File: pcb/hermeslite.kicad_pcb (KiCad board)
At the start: 4 copper layers, 49.9 x 49.9 mm, 71 parts, among them CN1 MEC6-140_CONNECTOR_BEMICRO, CN2 PCIE, CN4 SATA22, J1 0, J2 0, J3 0, J4 0, J5 0, P0 CONN_1, P12 CONN_1, P3 3V, P5 CONN_1, U1 AD9866BCPZ, U2 EEPROM, X1 61.440

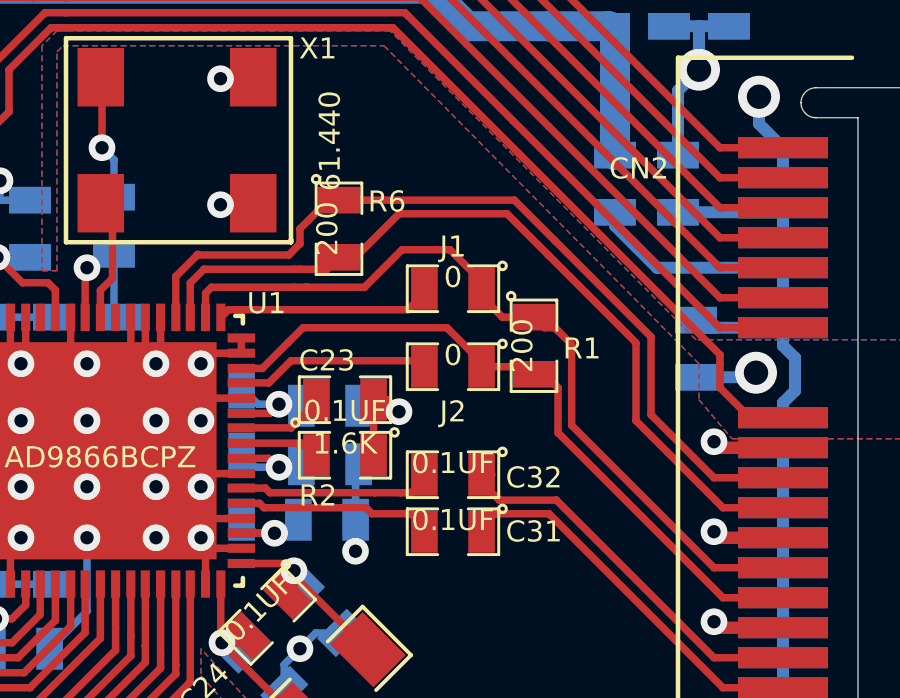
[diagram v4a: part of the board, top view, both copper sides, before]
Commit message: Updated BOM, renumbered a few references
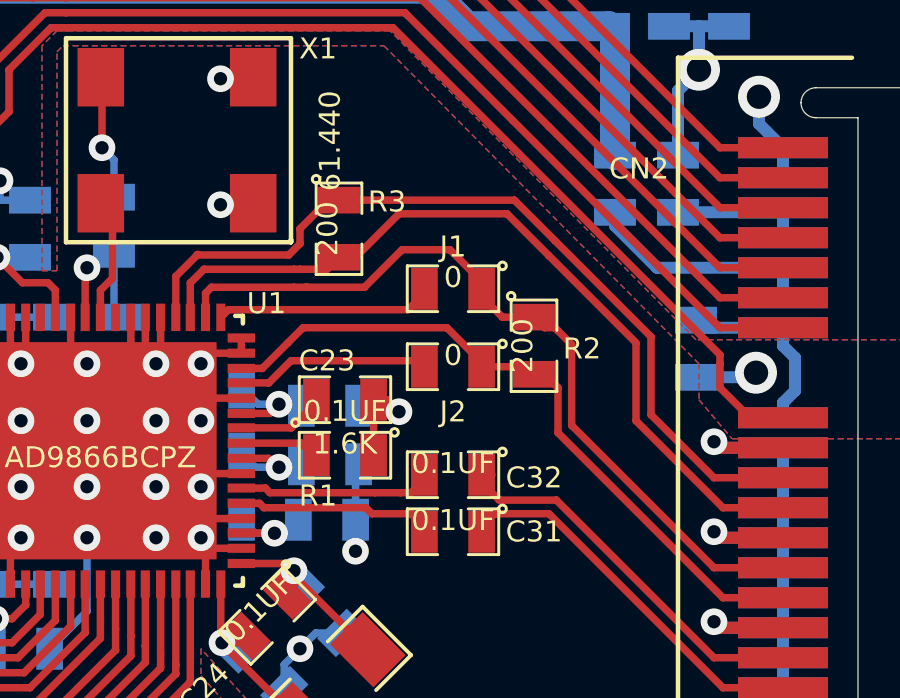
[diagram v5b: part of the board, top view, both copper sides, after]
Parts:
- P3: value 3V -> CONN_1
- renumbered CN4 to CN3, R2 to R1, R1 to R2, R6 to R3

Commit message: iTead Studio submission
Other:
- net class Default: clearance 0.205 -> 0
- rule trace_clearance: 0.205 -> 0
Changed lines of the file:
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@@
   (title_block
     (title Hermes-Lite)
-    (date "07 Oct 2014")
+    (date "08 Oct 2014")
     (rev 1,2)
     (company SofterHardware)
@@
   (layers
     (0 F.Cu signal)
-    (1 Inner2.Cu signal hide)
-    (2 Inner1.Cu signal hide)
-    (31 B.Cu signal hide)
+    (1 Inner2.Cu signal)
+    (2 Inner1.Cu signal)
+    (31 B.Cu signal)
     (32 B.Adhes user)
     (33 F.Adhes user)
@@
     (35 F.Paste user)
     (36 B.SilkS user)
-    (37 F.SilkS user hide)
+    (37 F.SilkS user)
     (38 B.Mask user)
     (39 F.Mask user)
@@
     (user_trace_width 0.4)
     (user_trace_width 1)
-    (trace_clearance 0.205)
+    (trace_clearance 0)
     (zone_clearance 0.45)
     (zone_45_only no)
@@
     (pad_drill 0.813)
     (pad_to_mask_clearance 0)
-    (aux_axis_origin 100.7 83.45)
+    (aux_axis_origin 100.7 83.2)
     (visible_elements FFFEFF7F)
     (pcbplotparams
-      (layerselection 0x01030_80000007)
+      (layerselection 0x010f0_80000007)
       (usegerberextensions true)
-      (excludeedgelayer true)
+      (excludeedgelayer false)
       (linewidth 0.150000)
       (plotframeref false)
@@
   (net 94 "Net-(R1-Pad2)")
   (net_class Default "This is the default net class."
-    (clearance 0.205)
+    (clearance 0)
     (trace_width 0.25)
     (via_dia 0.889)
@@
     (pad B18 smd rect (at -7.5 3.5 270) (size 0.7 3) (layers F.Cu F.Paste F.Mask)
       (net 81 /EXP_SCLK))
-    (pad A1 smd rect (at 11.5 3.5 270) (size 0.7 3) (layers B.Cu F.Paste F.Mask)
-      (net 5 GND))
-    (pad A2 smd rect (at 10.5 3.5 270) (size 0.7 3) (layers B.Cu F.Paste F.Mask)
-      (net 5 GND))
-    (pad A3 smd rect (at 9.5 3.5 270) (size 0.7 3) (layers B.Cu F.Paste F.Mask)
-      (net 5 GND))
-    (pad A4 smd rect (at 8.5 3.5 270) (size 0.7 3) (layers B.Cu F.Paste F.Mask)
-      (net 5 GND))
-    (pad A5 smd rect (at 7.5 3.5 270) (size 0.7 3) (layers B.Cu F.Paste F.Mask)
-      (net 5 GND))
-    (pad A6 smd rect (at 6.5 3.5 270) (size 0.7 3) (layers B.Cu F.Paste F.Mask)
-      (net 5 GND))
-    (pad A7 smd rect (at 5.5 3.5 270) (size 0.7 3) (layers B.Cu F.Paste F.Mask)
-      (net 5 GND))
-    (pad A8 smd rect (at 4.5 3.5 270) (size 0.7 3) (layers B.Cu F.Paste F.Mask)
-      (net 5 GND))
-    (pad A9 smd rect (at 3.5 3.5 270) (size 0.7 3) (layers B.Cu F.Paste F.Mask)
-      (net 5 GND))
-    (pad A10 smd rect (at 2.5 3.5 270) (size 0.7 3) (layers B.Cu F.Paste F.Mask)
-      (net 5 GND))
-    (pad A11 smd rect (at 1.5 3.5 270) (size 0.7 3) (layers B.Cu F.Paste F.Mask)
+    (pad A1 smd rect (at 11.5 3.5 270) (size 0.7 3) (layers B.Cu B.Paste B.Mask)
+      (net 5 GND))
+    (pad A2 smd rect (at 10.5 3.5 270) (size 0.7 3) (layers B.Cu B.Paste B.Mask)
+      (net 5 GND))
+    (pad A3 smd rect (at 9.5 3.5 270) (size 0.7 3) (layers B.Cu B.Paste B.Mask)
+      (net 5 GND))
+    (pad A4 smd rect (at 8.5 3.5 270) (size 0.7 3) (layers B.Cu B.Paste B.Mask)
+      (net 5 GND))
+    (pad A5 smd rect (at 7.5 3.5 270) (size 0.7 3) (layers B.Cu B.Paste B.Mask)
+      (net 5 GND))
+    (pad A6 smd rect (at 6.5 3.5 270) (size 0.7 3) (layers B.Cu B.Paste B.Mask)
+      (net 5 GND))
+    (pad A7 smd rect (at 5.5 3.5 270) (size 0.7 3) (layers B.Cu B.Paste B.Mask)
+      (net 5 GND))
+    (pad A8 smd rect (at 4.5 3.5 270) (size 0.7 3) (layers B.Cu B.Paste B.Mask)
+      (net 5 GND))
+    (pad A9 smd rect (at 3.5 3.5 270) (size 0.7 3) (layers B.Cu B.Paste B.Mask)
+      (net 5 GND))
+    (pad A10 smd rect (at 2.5 3.5 270) (size 0.7 3) (layers B.Cu B.Paste B.Mask)
+      (net 5 GND))
+    (pad A11 smd rect (at 1.5 3.5 270) (size 0.7 3) (layers B.Cu B.Paste B.Mask)
       (net 91 EXP12V))
-    (pad A12 smd rect (at -1.5 3.5 270) (size 0.7 3) (layers B.Cu F.Paste F.Mask)
+    (pad A12 smd rect (at -1.5 3.5 270) (size 0.7 3) (layers B.Cu B.Paste B.Mask)
       (net 91 EXP12V))
-    (pad A13 smd rect (at -2.5 3.5 270) (size 0.7 3) (layers B.Cu F.Paste F.Mask)
+    (pad A13 smd rect (at -2.5 3.5 270) (size 0.7 3) (layers B.Cu B.Paste B.Mask)
       (net 92 EXP5V))
-    (pad A14 smd rect (at -3.5 3.5 270) (size 0.7 3) (layers B.Cu F.Paste F.Mask)
+    (pad A14 smd rect (at -3.5 3.5 270) (size 0.7 3) (layers B.Cu B.Paste B.Mask)
       (net 92 EXP5V))
-    (pad A15 smd rect (at -4.5 3.5 270) (size 0.7 3) (layers B.Cu F.Paste F.Mask)
+    (pad A15 smd rect (at -4.5 3.5 270) (size 0.7 3) (layers B.Cu B.Paste B.Mask)
       (net 93 EXP3V))
-    (pad A16 smd rect (at -5.5 3.5 270) (size 0.7 3) (layers B.Cu F.Paste F.Mask)
+    (pad A16 smd rect (at -5.5 3.5 270) (size 0.7 3) (layers B.Cu B.Paste B.Mask)
       (net 93 EXP3V))
-    (pad A17 smd rect (at -6.5 3.5 270) (size 0.7 3) (layers B.Cu F.Paste F.Mask)
-      (net 5 GND))
-    (pad A18 smd rect (at -7.5 3.5 270) (size 0.7 3) (layers B.Cu F.Paste F.Mask)
+    (pad A17 smd rect (at -6.5 3.5 270) (size 0.7 3) (layers B.Cu B.Paste B.Mask)
+      (net 5 GND))
+    (pad A18 smd rect (at -7.5 3.5 270) (size 0.7 3) (layers B.Cu B.Paste B.Mask)
       (net 5 GND))
   )
@@
     (at 130.1 122 90)
     (attr smd)
-    (fp_text reference FB1 (at 2.7 0 180) (layer F.SilkS)
+    (fp_text reference FB1 (at 2.7 -0.4 180) (layer F.SilkS)
       (effects (font (size 0.7 0.7) (thickness 0.1)))
     )
@@
     (at 132.1 122 90)
     (attr smd)
-    (fp_text reference FB2 (at 2.7 0 180) (layer F.SilkS)
+    (fp_text reference FB2 (at 2.7 -0.3 180) (layer F.SilkS)
       (effects (font (size 0.7 0.7) (thickness 0.1)))
     )
@@
     (at 134.1 122 90)
     (attr smd)
-    (fp_text reference FB3 (at 2.7 0 180) (layer F.SilkS)
+    (fp_text reference FB3 (at 2.7 -0.1 180) (layer F.SilkS)
       (effects (font (size 0.7 0.7) (thickness 0.1)))
     )
@@
     (at 125.8 122 90)
     (attr smd)
-    (fp_text reference C16 (at 2.7 0 180) (layer F.SilkS)
+    (fp_text reference C16 (at 2.7 0.2 180) (layer F.SilkS)
       (effects (font (size 0.7 0.7) (thickness 0.1)))
     )
@@
   (via (at 102.375 104.025) (size 0.889) (layers F.Cu B.Cu) (net 5))
   (segment (start 104.2 104.0225) (end 102.3775 104.0225) (width 0.25) (layer F.Cu) (net 5))
-  (segment (start 102.2075 117.9925) (end 102.2 118) (width 0.25) (layer F.Cu) (net 5))
-  (via (at 102.2 118) (size 0.889) (layers F.Cu B.Cu) (net 5))
-  (segment (start 104.2 117.9925) (end 102.2075 117.9925) (width 0.25) (layer F.Cu) (net 5))
   (segment (start 105.1 113.9) (end 104.7 114.3) (width 0.25) (layer B.Cu) (net 5))
   (segment (start 104.7 114.3) (end 102.4 114.3) (width 0.25) (layer B.Cu) (net 5))
@@
   (via (at 136.4 125.5) (size 1.397) (drill 0.813) (layers F.Cu B.Cu) (net 5))
   (segment (start 137.715 128) (end 137.715 126.815) (width 0.4) (layer B.Cu) (net 5))
+  (segment (start 102.4075 117.9925) (end 102.4 118) (width 0.25) (layer F.Cu) (net 5))
+  (via (at 102.4 118) (size 0.889) (layers F.Cu B.Cu) (net 5))
+  (segment (start 104.2 117.9925) (end 102.4075 117.9925) (width 0.25) (layer F.Cu) (net 5))
   (segment (start 126.7 110.1) (end 126.473519 110.326481) (width 0.25) (layer F.Cu) (net 6))
   (segment (start 126.7 109.5) (end 126.7 110.1) (width 0.25) (layer F.Cu) (net 6))

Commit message: Added revision 1.21
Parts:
- removed PB3: CONN_1, Measurement_Points:Measurement_Point_Round-TH_Small
- added CN4: POWER, HERMESLITE:EDGE6, F.Cu at (141.4, 131.0)
- added FIDUCIAL: VAL**, HERMESLITE:FIDUCIAL, F.Cu at (148.5, 124.7)
- added FIDUCIAL: VAL**, HERMESLITE:FIDUCIAL, F.Cu at (102.7, 85.2)
- added FIDUCIAL: VAL**, HERMESLITE:FIDUCIAL, B.Cu at (102.7, 85.2)
- added FIDUCIAL: VAL**, HERMESLITE:FIDUCIAL, B.Cu at (148.5, 124.7)
- added G***: OSHW-logo_silkscreen-front_2mm, HERMESLITE:OSHW-logo_silkscreen-front_2mm, F.Cu at (136.6, 85.5)
- added G***: OSHW-logo_silkscreen-back_2mm, HERMESLITE:OSHW-logo_silkscreen-back_2mm, B.Cu at (115.5, 85.5)
- added J6: 0, SMD_Packages:SMD-0805, B.Cu at (108.7, 109.5)
- added J7: 0, HERMESLITE:JUMPER, F.Cu at (116.2, 121.3)
- added J8: 0, HERMESLITE:JUMPER, F.Cu at (116.8, 95.3)
- added P1: CONN_1, HERMESLITE:TH, F.Cu at (120.5, 105.5)
- added Palt0: CONN_1, Measurement_Points:Measurement_Point_Round-TH_Small, F.Cu at (127.0, 124.7)
- added S1: CONN_1, Measurement_Points:Measurement_Point_Round-TH_Small, F.Cu at (123.2, 126.5)
- added S2: CONN_1, Measurement_Points:Measurement_Point_Round-TH_Small, F.Cu at (125.0, 126.5)
- added S3: CONN_1, Measurement_Points:Measurement_Point_Round-TH_Small, F.Cu at (127.0, 126.5)
- added TP3: CONN_1, HERMESLITE:TP, F.Cu at (102.2, 105.9)
- added TP4: CONN_1, HERMESLITE:TP, F.Cu at (102.2, 107.5)
- added TP5: CONN_1, HERMESLITE:TP, F.Cu at (102.2, 108.8)
- added TP6: CONN_1, HERMESLITE:TP, F.Cu at (102.2, 119.0)
- CN3: value SATA22 -> GPIO; footprint HERMESLITE:SATA22 -> HERMESLITE:EDGE6; moved to F.Cu
- J5: footprint SMD_Packages:SMD-0805 -> HERMESLITE:JUMPER
- moved TP1 15.6 mm to (114.1, 118.3)
- moved J5 12.7 mm to (118.8, 123.8), turned to 90 degrees
- moved P3 11.4 mm to (136.4, 125.5)
- moved FB8 1.28 mm to (139.1, 102.9), turned to 180 degrees
- moved CN3 0.81 mm to (126.2, 131.0), turned to 270 degrees
- moved FB5 0.76 mm to (114.0, 92.3), turned to 0 degrees
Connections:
- net Net-(CN1-Pad24) renamed MSCK
- net Net-(CN1-Pad26) renamed MSI
- net Net-(CN1-Pad34) renamed MSO
- net Net-(CN1-Pad36) renamed MCSn
- CN1 pad 4: GND -> Net-(CN1-Pad4)
- FB5 pad 2: FPGA5V -> Net-(FB5-Pad2)
- J5 pad 2: GND -> Net-(CN1-Pad4)
- TP1 pad 1: Net-(CN1-Pad40) -> Net-(CN1-Pad7)
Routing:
- net Net-(CN1-Pad30): track 0.00 -> 31.2 mm, vias 0 -> 1
- net Net-(CN1-Pad28): track 0.00 -> 29.1 mm
- net Net-(CN1-Pad20): track 0.00 -> 26.7 mm, vias 0 -> 1
- net Net-(CN1-Pad9): track 0.00 -> 23.0 mm
- net Net-(CN1-Pad4): track 0.00 -> 18.5 mm, vias 0 -> 1
- net GND: track 299.7 -> 314.3 mm, vias 49 -> 39
- net Net-(CN1-Pad16): track 18.3 -> 26.8 mm
- net Net-(CN1-Pad18): track 19.7 -> 27.9 mm, vias 1 -> 0
- net Net-(CN1-Pad1): track 12.9 -> 20.5 mm, vias 0 -> 1
- net 3VIN: track 32.8 -> 39.9 mm
- net Net-(CN1-Pad14): track 18.2 -> 24.5 mm, vias 1 -> 0
- net Net-(CN3-Pad11): track 0.00 -> 5.78 mm
- net EXP12V: track 6.34 -> 11.8 mm
- net Net-(CN1-Pad12): track 16.4 -> 21.7 mm, vias 1 -> 0
- net Net-(CN3-Pad12): track 0.00 -> 4.81 mm
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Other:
- outline, holes or cut-outs redrawn
- board text added: "Hermes-Lite 1.21 © 2014 SofterHardware"
- board text removed: "F3V"
- board text removed: "Hermes-Lite 1.2 Copyright 2014 SofterHardware"

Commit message: Update to v1.22
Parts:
- X1: value 61.440 -> 73.728
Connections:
- net /EXP_GPIO0 renamed /USEROUT0
- net /EXP_GPIO1 renamed /USEROUT1
- net /EXP_GPIO2 renamed /USEROUT2
- net /EXP_SCLK renamed /USEROUT6
- net /EXP_SDI renamed /USEROUT4
- net /EXP_SDO renamed /USEROUT5
- net /EXP_SEN renamed /USEROUT3
- U1 pad 53: GND -> Net-(CN1-Pad67)
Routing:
- net Net-(CN1-Pad67): track 2.01 -> 17.7 mm
- net GND: track 314.3 -> 311.7 mm
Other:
- board text added: "Hermes-Lite 1.22 © 2015 SofterHardware"
- board text removed: "Hermes-Lite 1.21 © 2014 SofterHardware"
